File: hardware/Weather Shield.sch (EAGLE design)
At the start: 50 parts, among them Q1 BSS138, Q2 BSS138, U1 ARDUINO_R3_SHIELD, U2 3.3V MIC5219, U3 ALS-PT19, U4 MPL3115A2LGA8, U5 HTU21D, U7 GP-635T, U8 TEMT6000

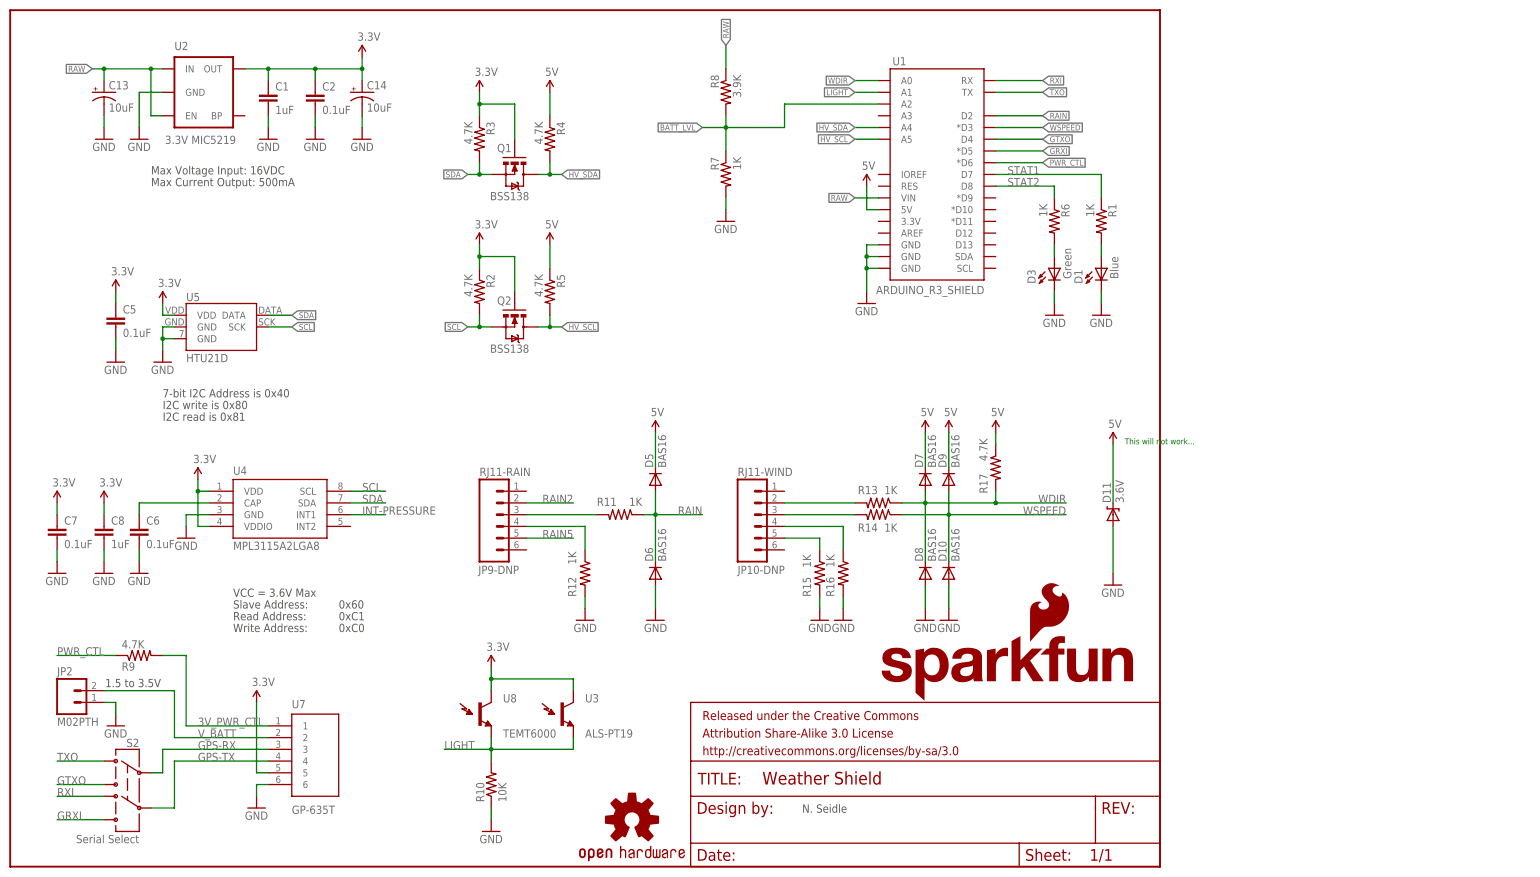
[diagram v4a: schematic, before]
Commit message: v1.1 that addresses many issues.
Many schematic and routing changes. See issues.
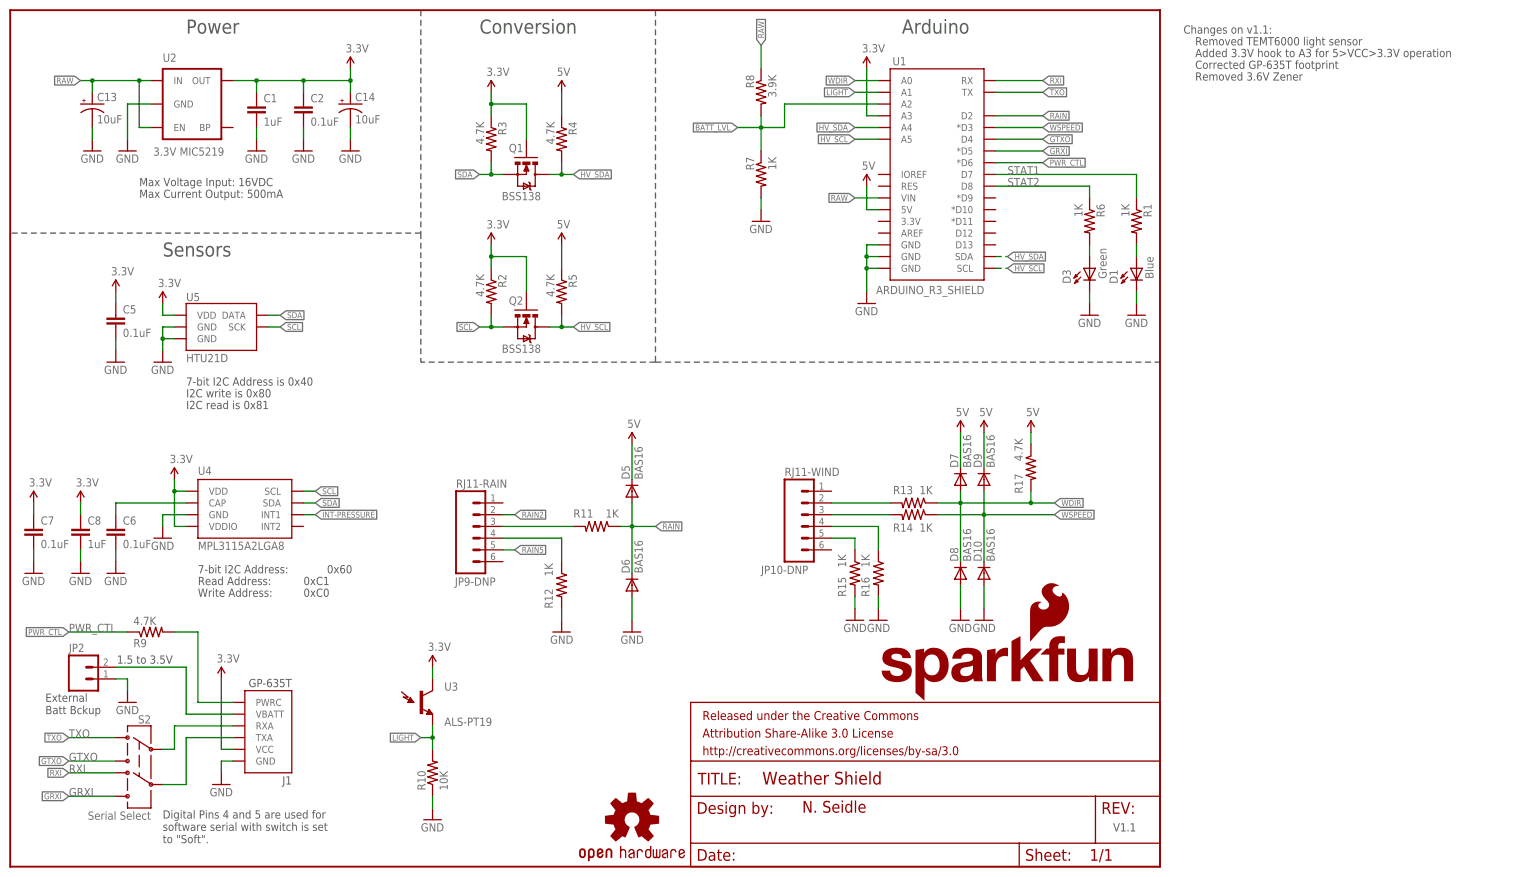
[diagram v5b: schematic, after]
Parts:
- removed D11: 3.6V, SparkFun:DIODE-ZENER-BZT52
- removed U7: GP-635T, SparkFun-Connectors:JST_VERTICAL
- removed U8: TEMT6000, SparkFun-Sensors:TEMT6000
- added J1: GP-635T, SparkFun-Sensors:GP-635TSMD
- JP2: value M02PTH -> External Batt Bckup
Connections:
- net 3.3V: now also J1.VCC, U1.A3; no longer U7.5, U8.C1
- net 3V_PWR_CTL: now also J1.PWRC; no longer U7.1
- net 5V: no longer D11.C
- net GND: now also J1.GND; no longer D11.A, U7.6
- net GPS-RX: now also J1.RXA; no longer U7.3
- net GPS-TX: now also J1.TXA; no longer U7.4
- net HV_SCL: now also U1.SCL
- net HV_SDA: now also U1.SDA
- net LIGHT: no longer U8.E1
- net V_BATT: now also J1.VBATT; no longer U7.2
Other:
- note added: "7-bit I2C Address:"
- note added: "Added 3.3V hook to A3 for 5>VCC>3.3V operation"
- note added: "Arduino"
- note added: "Changes on v1.1:"
- note added: "Conversion"
- note added: "Corrected GP-635T footprint"
- note added: "Digital Pins 4 and 5 are used for software serial with switch is set to "Soft"."
- note added: "External Batt Bckup"
- note added: "GPS (optional)"
- note added: "Humidity"
- note added: "Light"
- note added: "Power"
- note added: "Pressure"
- note added: "Removed 3.6V Zener"
- note added: "Removed TEMT6000 light sensor"
- note added: "Sensors"
- note added: "V1.1"
- note removed: "Slave Address:"
- note removed: "This will not work..."
- note removed: "VCC = 3.6V Max"
- moved on the sheet: C1, C13, C14, C2, C6, C7, C8, D1, D10, D3, D5, D6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
